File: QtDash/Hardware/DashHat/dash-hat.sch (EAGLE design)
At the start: 163 parts, among them IC1 LMV614, IC2 MCP3X083008, IC3 MCP23017SS, IC4 LM358D, IC5 IL300, IC6 TSV912D, IC7 IL300, IC8 TSV912D, IC9 DS1374, J1 CONN_20X2, J10 455-1750-1-ND, J11 455-1750-1-ND, J15 VSS_IN, J16 TACH_IN, J6 VOLVO_CONN_31, J7 VOLVO_CONN_32, J8 455-1750-1-ND, J9 455-1750-1-ND, Y1 ECX-.327-6-34RR

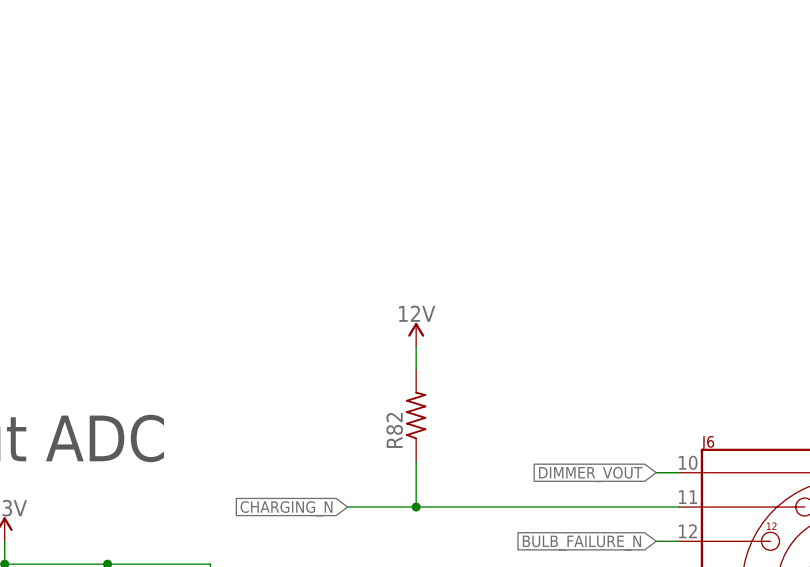
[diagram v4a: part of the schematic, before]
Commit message: bugfix/hardware-revA-issues: 	- moved alternator D+ supply to fuse 16 12V supply 	- added datasheet for new LED backlit screen 	- added mount stls
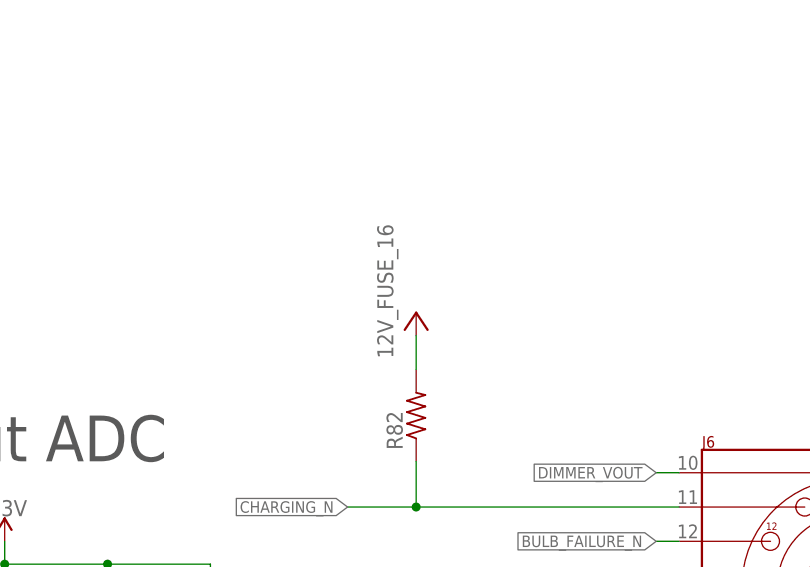
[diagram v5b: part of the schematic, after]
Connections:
- net 12V: no longer R82.2
- net 12V-FUSE_16: now also R82.2
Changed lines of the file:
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@@
 <setting verticaltext="up"/>
 </settings>
-<grid distance="0.1" unitdist="inch" unit="inch" style="lines" multiple="1" display="no" altdistance="0.01" altunitdist="inch" altunit="inch"/>
+<grid distance="0.05" unitdist="inch" unit="inch" style="lines" multiple="1" display="no" altdistance="0.01" altunitdist="inch" altunit="inch"/>
 <layers>
 <layer number="1" name="Top" color="4" fill="1" visible="no" active="no"/>
@@
 <part name="R78" library="digital_dash" deviceset="RC0603JR" device="" technology="-071KL" value="1k"/>
 <part name="R79" library="digital_dash" deviceset="RC0603JR" device="" technology="-071KL" value="1k"/>
-<part name="SUPPLY56" library="SparkFun-PowerSymbols" deviceset="12V" device=""/>
 <part name="R82" library="resistor" deviceset="R-US_" device="0617/17"/>
+<part name="U$4" library="digital_dash" deviceset="12V_FUSE_16" device=""/>
 </parts>
 <sheets>
@@
 <instance part="R78" gate="G$1" x="497.84" y="156.21" rot="R90"/>
 <instance part="R79" gate="G$1" x="497.84" y="143.51" rot="R90"/>
-<instance part="SUPPLY56" gate="G$1" x="454.66" y="288.29"/>
 <instance part="R82" gate="G$1" x="454.66" y="280.67" rot="R90"/>
+<instance part="U$4" gate="G$1" x="454.66" y="289.56"/>
 </instances>
 <busses>
@@
 <wire x1="203.2" y1="219.71" x2="203.2" y2="226.06" width="0.1524" layer="91"/>
 </segment>
-<segment>
-<pinref part="SUPPLY56" gate="G$1" pin="12V"/>
-<pinref part="R82" gate="G$1" pin="2"/>
-<wire x1="454.66" y1="285.75" x2="454.66" y2="288.29" width="0.1524" layer="91"/>
-</segment>
 </net>
 <net name="OUT1" class="0">
@@
 <pinref part="U$2" gate="G$1" pin="12V-FUSE_16"/>
 </segment>
+<segment>
+<pinref part="R82" gate="G$1" pin="2"/>
+<pinref part="U$4" gate="G$1" pin="12V-FUSE_16"/>
+<wire x1="454.66" y1="285.75" x2="454.66" y2="289.56" width="0.1524" layer="91"/>
+</segment>
 </net>

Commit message: bugfix/hardware-revA-issues: 	- added outputs solder points for fuse 16 and fuse 8 power 	- added 12V input solder points switched power? 	- added some ground vias on for 5V ground return path -- things were a little tight 	- extended board to add output power solder points
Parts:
- removed J11, J9: 455-1750-1-ND, SparkFun-Connectors:CONN_03
- removed JP21: JUMPER-SMT_3_NO_SILK, SparkFun-Jumpers:JUMPER-SMT_3_NO_SILK
- added J17, J18, J19, J20, J21, J22: (no value), SparkFun-Connectors:CONN_02PTH4
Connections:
- removed net N$10: J11.1, J9.1, JP21.3
- removed net N$12: J11.2, J9.2
- removed net N$14: J11.3, J9.3, JP21.1
- net 12V: now also J18.1, J18.2; no longer JP21.2
- net 12V-FUSE_16: now also J17.1, J17.2
- net 12V-FUSE_8: now also J22.1, J22.2
- net 5V: now also J19.2
- net GND: now also J19.1
- net GND-ISO: now also J20.1, J20.2, J21.1, J21.2
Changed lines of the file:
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@@
 <part name="D5" library="diode" deviceset="BAT54S" device=""/>
 <part name="D6" library="diode" deviceset="BAT54S" device=""/>
-<part name="J9" library="SparkFun-Connectors" deviceset="CONN_03" device="" value="455-1750-1-ND"/>
-<part name="J11" library="SparkFun-Connectors" deviceset="CONN_03" device="" value="455-1750-1-ND"/>
-<part name="JP21" library="SparkFun-Jumpers" deviceset="JUMPER-SMT_3_NO" device="_SILK"/>
 <part name="SUPPLY51" library="SparkFun-PowerSymbols" deviceset="12V" device=""/>
 <part name="JP22" library="SparkFun-Jumpers" deviceset="JUMPER-SMT_3_NO" device="_SILK" value="SPI_CS_SEL"/>
@@
 <part name="R82" library="resistor" deviceset="R-US_" device="0617/17"/>
 <part name="U$4" library="digital_dash" deviceset="12V_FUSE_16" device=""/>
+<part name="J19" library="SparkFun-Connectors" deviceset="CONN_02" device="PTH4"/>
+<part name="SUPPLY56" library="SparkFun-PowerSymbols" deviceset="5V" device=""/>
+<part name="GND51" library="SparkFun-PowerSymbols" deviceset="GND" device=""/>
+<part name="J20" library="SparkFun-Connectors" deviceset="CONN_02" device="PTH4"/>
+<part name="J21" library="SparkFun-Connectors" deviceset="CONN_02" device="PTH4"/>
+<part name="GND-ISO26" library="SparkFun-PowerSymbols" deviceset="GND-ISO" device=""/>
+<part name="J22" library="SparkFun-Connectors" deviceset="CONN_02" device="PTH4"/>
+<part name="J17" library="SparkFun-Connectors" deviceset="CONN_02" device="PTH4"/>
+<part name="J18" library="SparkFun-Connectors" deviceset="CONN_02" device="PTH4"/>
 </parts>
 <sheets>
@@
 <instance part="D5" gate="G$1" x="35.56" y="173.99" rot="R90"/>
 <instance part="D6" gate="G$1" x="35.56" y="137.16" rot="R90"/>
-<instance part="J9" gate="J$1" x="398.78" y="151.13"/>
-<instance part="J11" gate="J$1" x="449.58" y="151.13" rot="MR0"/>
-<instance part="JP21" gate="G$1" x="421.64" y="166.37" rot="R270"/>
 <instance part="SUPPLY51" gate="G$1" x="421.64" y="176.53"/>
 <instance part="JP22" gate="G$1" x="69.85" y="27.94" rot="R180"/>
@@
 <instance part="R82" gate="G$1" x="454.66" y="280.67" rot="R90"/>
 <instance part="U$4" gate="G$1" x="454.66" y="289.56"/>
+<instance part="J19" gate="G$1" x="66.04" y="72.39"/>
+<instance part="SUPPLY56" gate="G$1" x="76.2" y="80.01"/>
+<instance part="GND51" gate="1" x="76.2" y="66.04"/>
+<instance part="J20" gate="G$1" x="147.32" y="175.26"/>
+<instance part="J21" gate="G$1" x="147.32" y="165.1"/>
+<instance part="GND-ISO26" gate="G$1" x="158.75" y="157.48"/>
+<instance part="J22" gate="G$1" x="567.69" y="274.32" rot="R180"/>
+<instance part="J17" gate="G$1" x="441.96" y="218.44"/>
+<instance part="J18" gate="G$1" x="411.48" y="165.1"/>
 </instances>
 <busses>
@@
 <junction x="538.48" y="137.16"/>
 </segment>
+<segment>
+<pinref part="J19" gate="G$1" pin="1"/>
+<wire x1="73.66" y1="72.39" x2="76.2" y2="72.39" width="0.1524" layer="91"/>
+<wire x1="76.2" y1="72.39" x2="76.2" y2="68.58" width="0.1524" layer="91"/>
+<pinref part="GND51" gate="1" pin="GND"/>
+</segment>
 </net>
 <net name="5V" class="0">
@@
 <pinref part="SUPPLY6" gate="G$1" pin="5V"/>
 <wire x1="31.75" y1="328.93" x2="31.75" y2="326.39" width="0.1524" layer="91"/>
+</segment>
+<segment>
+<pinref part="J19" gate="G$1" pin="2"/>
+<wire x1="73.66" y1="74.93" x2="76.2" y2="74.93" width="0.1524" layer="91"/>
+<wire x1="76.2" y1="74.93" x2="76.2" y2="80.01" width="0.1524" layer="91"/>
+<pinref part="SUPPLY56" gate="G$1" pin="5V"/>
 </segment>
 </net>
@@
 </segment>
 <segment>
-<pinref part="JP21" gate="G$1" pin="2"/>
-<wire x1="421.64" y1="171.45" x2="421.64" y2="176.53" width="0.1524" layer="91"/>
-<pinref part="SUPPLY51" gate="G$1" pin="12V"/>
-</segment>
-<segment>
 <pinref part="D7" gate="G$1" pin="C2"/>
 <pinref part="SUPPLY38" gate="G$1" pin="12V"/>
@@
 <pinref part="SUPPLY43" gate="G$1" pin="12V"/>
 <wire x1="203.2" y1="219.71" x2="203.2" y2="226.06" width="0.1524" layer="91"/>
+</segment>
+<segment>
+<pinref part="J18" gate="G$1" pin="2"/>
+<pinref part="SUPPLY51" gate="G$1" pin="12V"/>
+<wire x1="419.1" y1="167.64" x2="421.64" y2="167.64" width="0.1524" layer="91"/>
+<wire x1="421.64" y1="167.64" x2="421.64" y2="176.53" width="0.1524" layer="91"/>
+<pinref part="J18" gate="G$1" pin="1"/>
+<wire x1="419.1" y1="165.1" x2="421.64" y2="165.1" width="0.1524" layer="91"/>
+<wire x1="421.64" y1="165.1" x2="421.64" y2="167.64" width="0.1524" layer="91"/>
+<junction x="421.64" y="167.64"/>
 </segment>
 </net>
@@
 <wire x1="203.2" y1="203.2" x2="203.2" y2="209.55" width="0.1524" layer="91"/>
 </segment>
+<segment>
+<pinref part="J20" gate="G$1" pin="1"/>
+<wire x1="154.94" y1="175.26" x2="158.75" y2="175.26" width="0.1524" layer="91"/>
+<wire x1="158.75" y1="175.26" x2="158.75" y2="167.64" width="0.1524" layer="91"/>
+<pinref part="J21" gate="G$1" pin="1"/>
+<wire x1="158.75" y1="167.64" x2="158.75" y2="165.1" width="0.1524" layer="91"/>
+<wire x1="158.75" y1="165.1" x2="158.75" y2="160.02" width="0.1524" layer="91"/>
+<wire x1="154.94" y1="165.1" x2="158.75" y2="165.1" width="0.1524" layer="91"/>
+<junction x="158.75" y="165.1"/>
+<pinref part="J21" gate="G$1" pin="2"/>
+<wire x1="154.94" y1="167.64" x2="158.75" y2="167.64" width="0.1524" layer="91"/>
+<junction x="158.75" y="167.64"/>
+<pinref part="J20" gate="G$1" pin="2"/>
+<wire x1="154.94" y1="177.8" x2="158.75" y2="177.8" width="0.1524" layer="91"/>
+<wire x1="158.75" y1="177.8" x2="158.75" y2="175.26" width="0.1524" layer="91"/>
+<junction x="158.75" y="175.26"/>
+<pinref part="GND-ISO26" gate="G$1" pin="GND-ISO"/>
+</segment>
 </net>
 <net name="BRAKE_FAILURE_N" class="0">
@@
 <pinref part="J6" gate="G$1" pin="9"/>
 <wire x1="523.24" y1="270.51" x2="525.78" y2="270.51" width="0.1524" layer="91"/>
-<wire x1="525.78" y1="270.51" x2="525.78" y2="279.4" width="0.1524" layer="91"/>
+<wire x1="525.78" y1="270.51" x2="525.78" y2="274.32" width="0.1524" layer="91"/>
 <pinref part="U$1" gate="G$1" pin="12V-FUSE_8"/>
+<wire x1="525.78" y1="274.32" x2="525.78" y2="279.4" width="0.1524" layer="91"/>
+<wire x1="560.07" y1="274.32" x2="556.26" y2="274.32" width="0.1524" layer="91"/>
+<junction x="525.78" y="274.32"/>
+<pinref part="J22" gate="G$1" pin="1"/>
+<pinref part="J22" gate="G$1" pin="2"/>
+<wire x1="556.26" y1="274.32" x2="525.78" y2="274.32" width="0.1524" layer="91"/>
+<wire x1="560.07" y1="271.78" x2="556.26" y2="271.78" width="0.1524" layer="91"/>
+<wire x1="556.26" y1="271.78" x2="556.26" y2="274.32" width="0.1524" layer="91"/>
+<junction x="556.26" y="274.32"/>
 </segment>
 <segment>
@@
 <wire x1="480.06" y1="220.98" x2="480.06" y2="233.68" width="0.1524" layer="91"/>
 <pinref part="U$2" gate="G$1" pin="12V-FUSE_16"/>
+<wire x1="480.06" y1="220.98" x2="452.12" y2="220.98" width="0.1524" layer="91"/>
+<junction x="480.06" y="220.98"/>
+<pinref part="J17" gate="G$1" pin="2"/>
+<pinref part="J17" gate="G$1" pin="1"/>
+<wire x1="452.12" y1="220.98" x2="449.58" y2="220.98" width="0.1524" layer="91"/>
+<wire x1="449.58" y1="218.44" x2="452.12" y2="218.44" width="0.1524" layer="91"/>
+<wire x1="452.12" y1="218.44" x2="452.12" y2="220.98" width="0.1524" layer="91"/>
+<junction x="452.12" y="220.98"/>
 </segment>
 <segment>
@@
 </segment>
 </net>
-<net name="N$10" class="0">
-<segment>
-<pinref part="J9" gate="J$1" pin="1"/>
-<pinref part="J11" gate="J$1" pin="1"/>
-<wire x1="406.4" y1="148.59" x2="415.29" y2="148.59" width="0.1524" layer="91"/>
-<wire x1="415.29" y1="148.59" x2="441.96" y2="148.59" width="0.1524" layer="91"/>
-<wire x1="415.29" y1="148.59" x2="415.29" y2="166.37" width="0.1524" layer="91"/>
-<junction x="415.29" y="148.59"/>
-<pinref part="JP21" gate="G$1" pin="3"/>
-<wire x1="415.29" y1="166.37" x2="416.56" y2="166.37" width="0.1524" layer="91"/>
-</segment>
-</net>
-<net name="N$12" class="0">
-<segment>
-<pinref part="J9" gate="J$1" pin="2"/>
-<pinref part="J11" gate="J$1" pin="2"/>
-<wire x1="406.4" y1="151.13" x2="441.96" y2="151.13" width="0.1524" layer="91"/>
-</segment>
-</net>
-<net name="N$14" class="0">
-<segment>
-<pinref part="J9" gate="J$1" pin="3"/>
-<pinref part="J11" gate="J$1" pin="3"/>
-<wire x1="406.4" y1="153.67" x2="427.99" y2="153.67" width="0.1524" layer="91"/>
-<wire x1="427.99" y1="153.67" x2="441.96" y2="153.67" width="0.1524" layer="91"/>
-<wire x1="427.99" y1="153.67" x2="427.99" y2="166.37" width="0.1524" layer="91"/>
-<junction x="427.99" y="153.67"/>
-<pinref part="JP21" gate="G$1" pin="1"/>
-<wire x1="427.99" y1="166.37" x2="426.72" y2="166.37" width="0.1524" layer="91"/>
-</segment>
-</net>

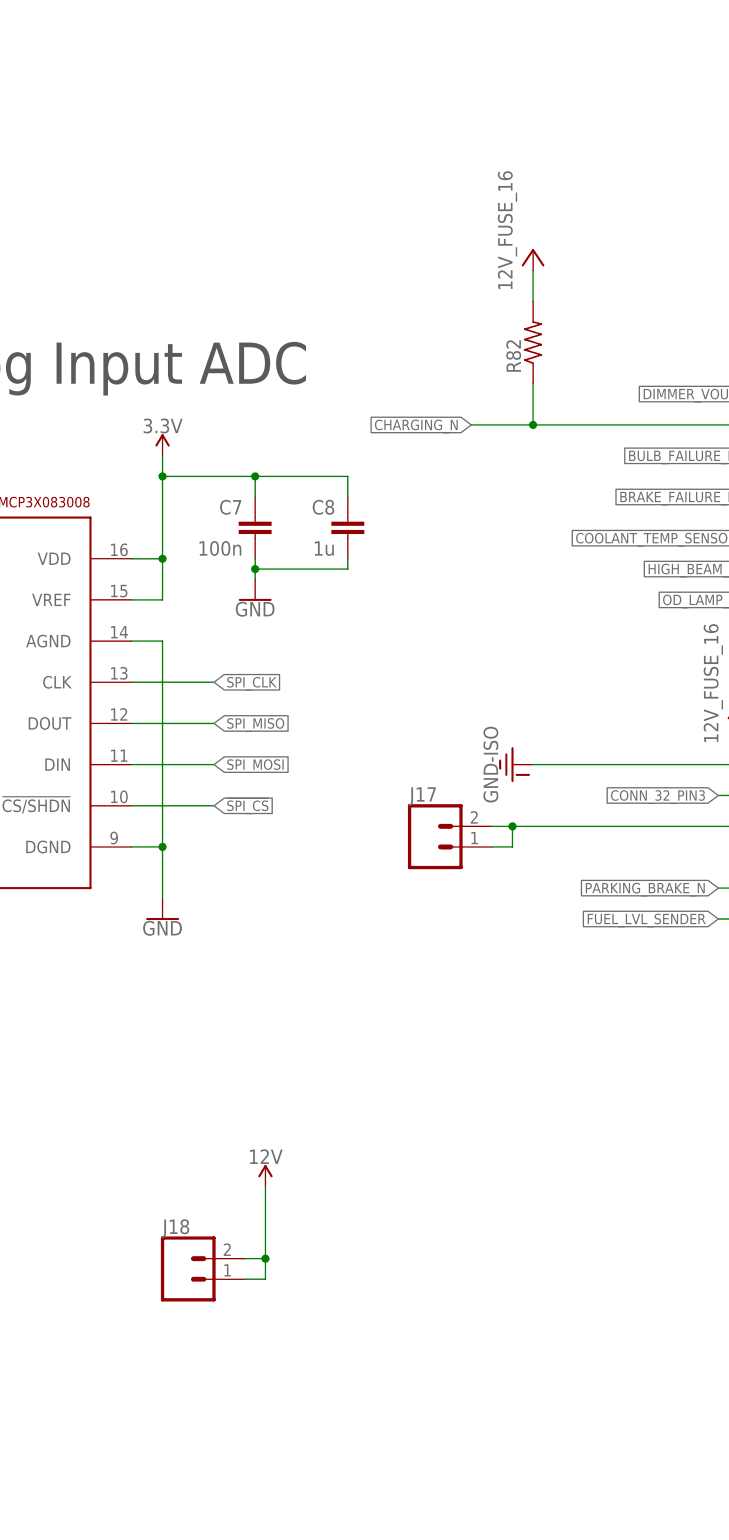
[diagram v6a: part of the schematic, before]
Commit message: bugfix/hardware-revA-issues: 	- moved D+ resistor back to switched 12V supply 	- added second switched 12V header 	- D+ resistor moved and 12Vin plane extended
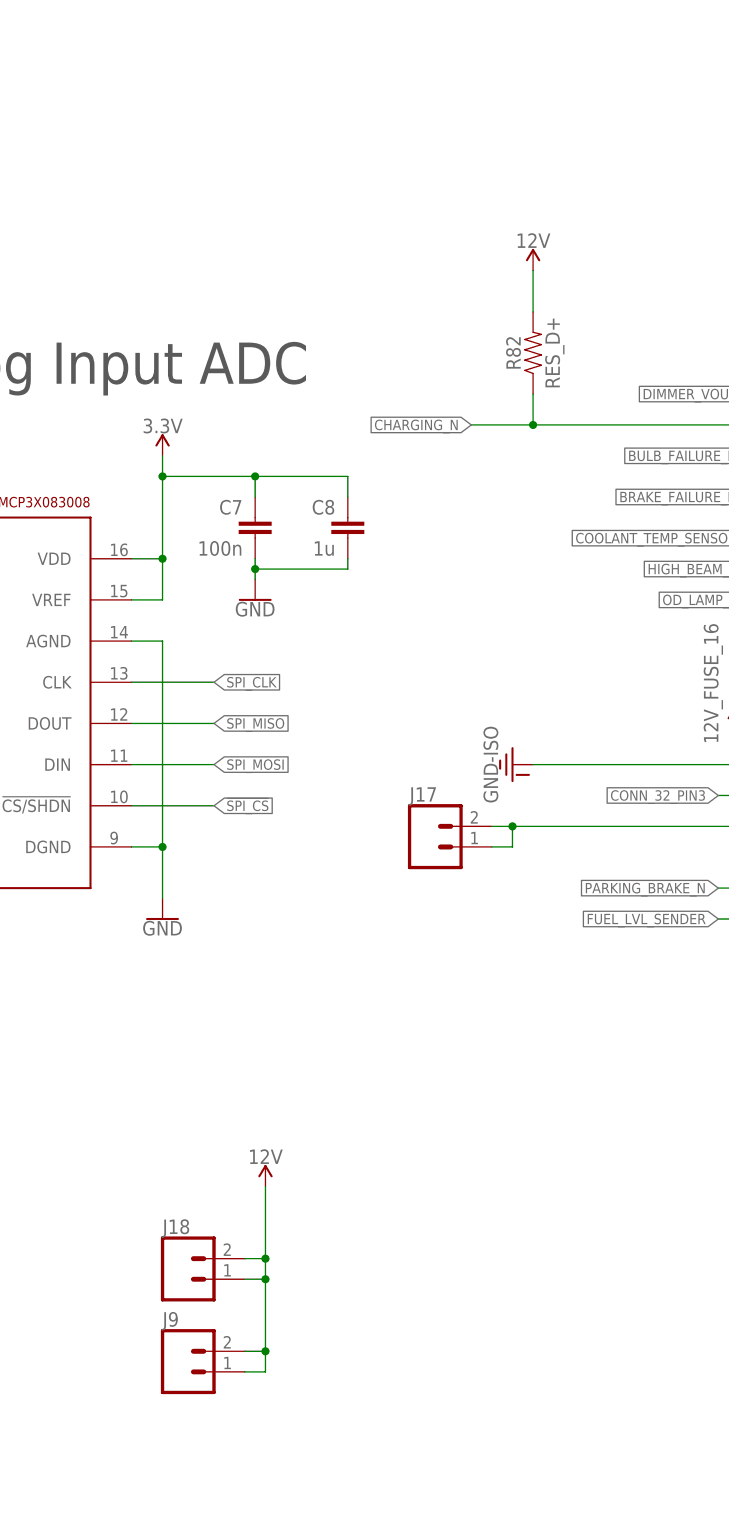
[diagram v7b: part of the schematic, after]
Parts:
- added J9: (no value), SparkFun-Connectors:CONN_02PTH4
- R82: value (none) -> RES_D+; device resistor:R-US_0617/17 -> digital_dash:RES_D+
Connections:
- net 12V: now also J9.1, J9.2, R82.2
- net 12V-FUSE_16: no longer R82.2
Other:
- moved on the sheet: R82
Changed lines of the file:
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@@
 <part name="R78" library="digital_dash" deviceset="RC0603JR" device="" technology="-071KL" value="1k"/>
 <part name="R79" library="digital_dash" deviceset="RC0603JR" device="" technology="-071KL" value="1k"/>
-<part name="R82" library="resistor" deviceset="R-US_" device="0617/17"/>
-<part name="U$4" library="digital_dash" deviceset="12V_FUSE_16" device=""/>
+<part name="R82" library="digital_dash" deviceset="RES_D+" device=""/>
 <part name="J19" library="SparkFun-Connectors" deviceset="CONN_02" device="PTH4"/>
 <part name="SUPPLY56" library="SparkFun-PowerSymbols" deviceset="5V" device=""/>
@@
 <part name="J17" library="SparkFun-Connectors" deviceset="CONN_02" device="PTH4"/>
 <part name="J18" library="SparkFun-Connectors" deviceset="CONN_02" device="PTH4"/>
+<part name="SUPPLY57" library="SparkFun-PowerSymbols" deviceset="12V" device=""/>
+<part name="J9" library="SparkFun-Connectors" deviceset="CONN_02" device="PTH4"/>
 </parts>
 <sheets>
@@
 <instance part="R78" gate="G$1" x="497.84" y="156.21" rot="R90"/>
 <instance part="R79" gate="G$1" x="497.84" y="143.51" rot="R90"/>
-<instance part="R82" gate="G$1" x="454.66" y="280.67" rot="R90"/>
-<instance part="U$4" gate="G$1" x="454.66" y="289.56"/>
+<instance part="R82" gate="G$1" x="454.66" y="279.4" rot="R90"/>
 <instance part="J19" gate="G$1" x="66.04" y="72.39"/>
 <instance part="SUPPLY56" gate="G$1" x="76.2" y="80.01"/>
@@
 <instance part="J17" gate="G$1" x="441.96" y="218.44"/>
 <instance part="J18" gate="G$1" x="411.48" y="165.1"/>
+<instance part="SUPPLY57" gate="G$1" x="454.66" y="289.56"/>
+<instance part="J9" gate="G$1" x="411.48" y="153.67"/>
 </instances>
 <busses>
@@
 <wire x1="421.64" y1="165.1" x2="421.64" y2="167.64" width="0.1524" layer="91"/>
 <junction x="421.64" y="167.64"/>
+<pinref part="J9" gate="G$1" pin="2"/>
+<wire x1="419.1" y1="156.21" x2="421.64" y2="156.21" width="0.1524" layer="91"/>
+<wire x1="421.64" y1="156.21" x2="421.64" y2="165.1" width="0.1524" layer="91"/>
+<junction x="421.64" y="165.1"/>
+<pinref part="J9" gate="G$1" pin="1"/>
+<wire x1="419.1" y1="153.67" x2="421.64" y2="153.67" width="0.1524" layer="91"/>
+<wire x1="421.64" y1="153.67" x2="421.64" y2="156.21" width="0.1524" layer="91"/>
+<junction x="421.64" y="156.21"/>
+</segment>
+<segment>
+<pinref part="R82" gate="G$1" pin="2"/>
+<pinref part="SUPPLY57" gate="G$1" pin="12V"/>
+<wire x1="454.66" y1="284.48" x2="454.66" y2="289.56" width="0.1524" layer="91"/>
 </segment>
 </net>
@@
 <label x="447.04" y="270.51" size="1.27" layer="95" rot="R180" xref="yes"/>
 <wire x1="454.66" y1="270.51" x2="447.04" y2="270.51" width="0.1524" layer="91"/>
-<wire x1="454.66" y1="275.59" x2="454.66" y2="270.51" width="0.1524" layer="91"/>
+<wire x1="454.66" y1="274.32" x2="454.66" y2="270.51" width="0.1524" layer="91"/>
 <junction x="454.66" y="270.51"/>
 <pinref part="R82" gate="G$1" pin="1"/>
@@
 <junction x="452.12" y="220.98"/>
 </segment>
-<segment>
-<pinref part="R82" gate="G$1" pin="2"/>
-<pinref part="U$4" gate="G$1" pin="12V-FUSE_16"/>
-<wire x1="454.66" y1="285.75" x2="454.66" y2="289.56" width="0.1524" layer="91"/>
-</segment>
-</net>
+</net>
